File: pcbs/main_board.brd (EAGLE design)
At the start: 120 x 20 mm, 41 parts, among them IC1 317T, IC2 MEGA48/88/168-AU, J1 22-27-2021-02, K1 G6K-2F, Q1 MOSFET-NCHANNELSMD, Q2 MOSFET-NCHANNELSMD

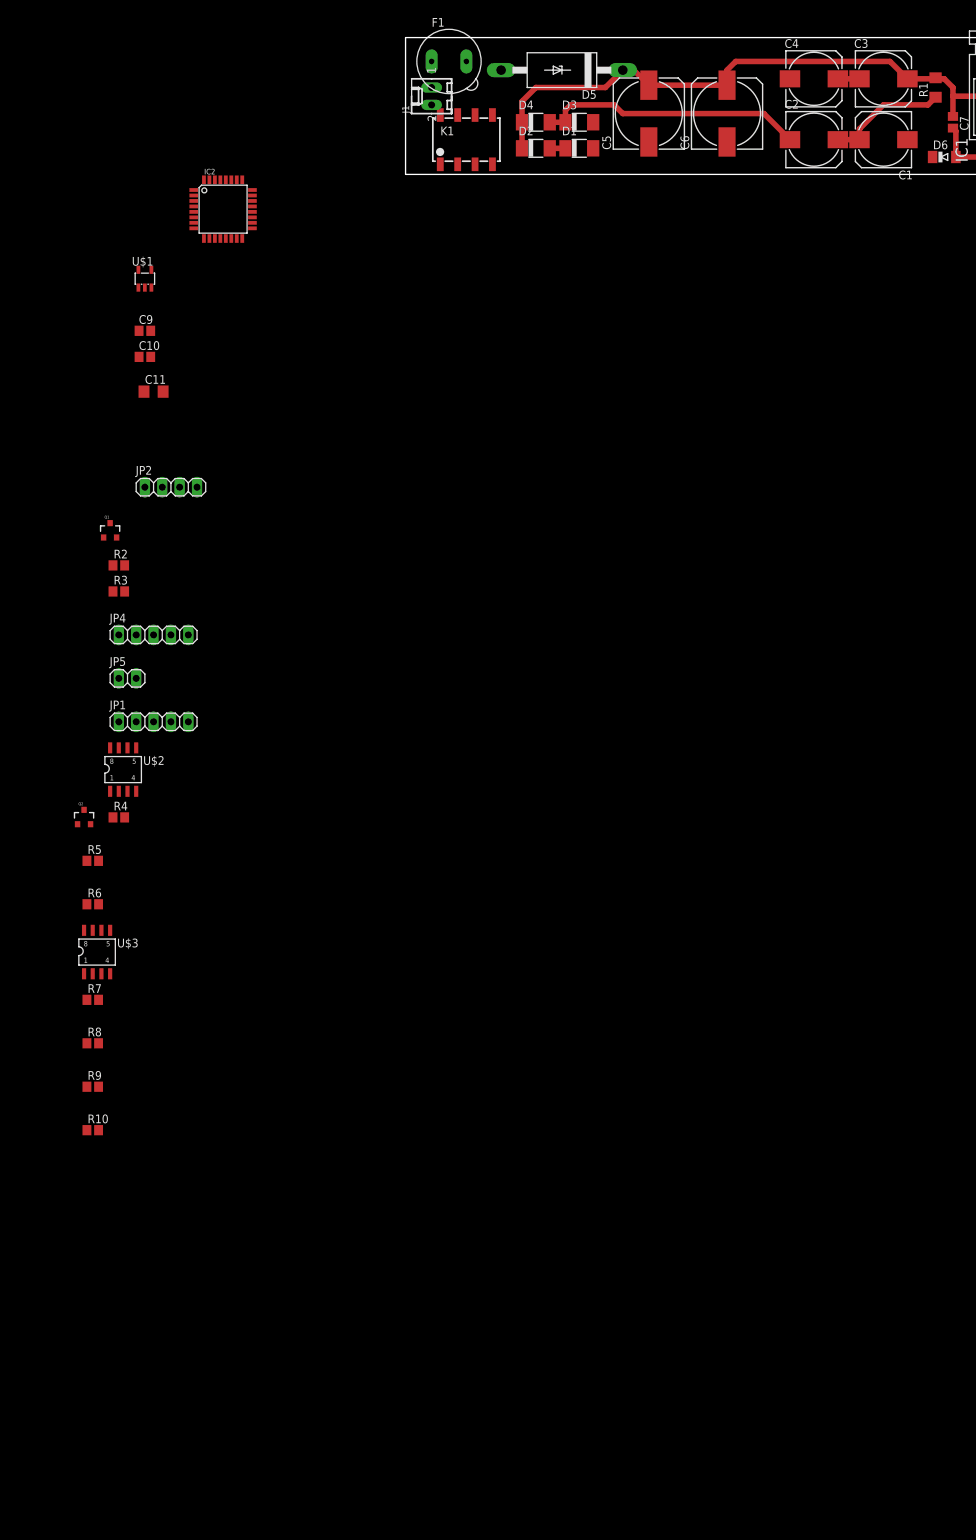
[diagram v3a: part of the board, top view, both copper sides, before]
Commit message: Main Board: Added resistor dividers for voltage measurements.
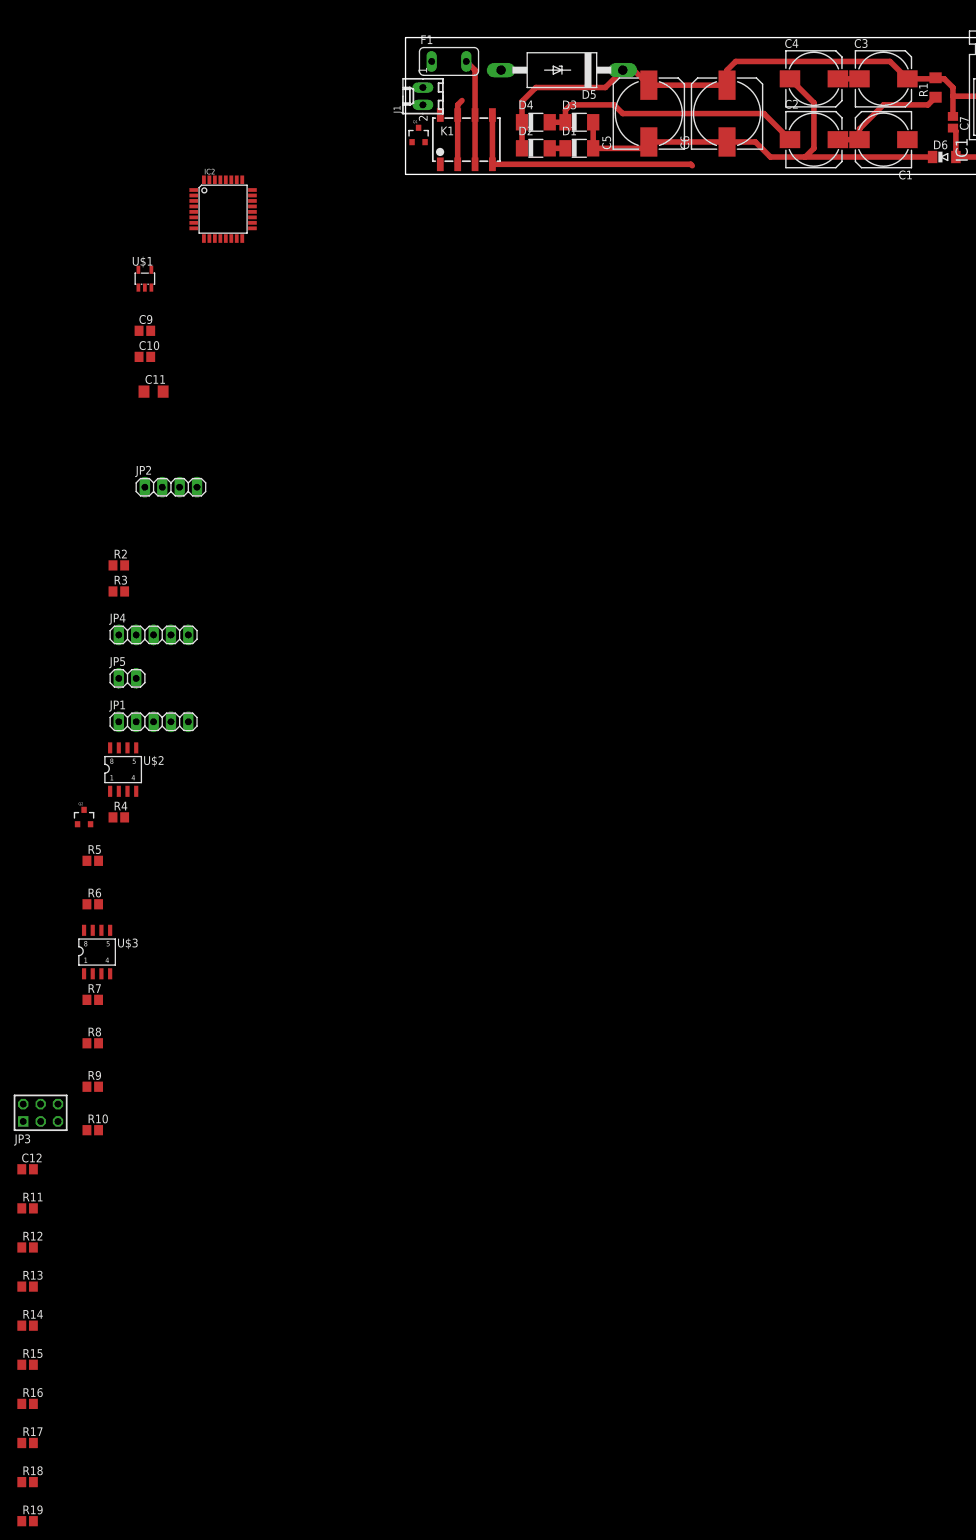
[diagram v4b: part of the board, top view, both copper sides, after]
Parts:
- added C12: 10n, resistor:C0805
- added JP3: AVR-ISP-6VERT, ShortCircuitRobotics:AVR-ISP-6
- added R11, R12, R13, R14, R15, R16, R17, R18: 1k, resistor:R0805
- added R19: 100k, resistor:R0805
- F1: value FUSE19560 -> (none); device fuse:19560 -> fuse:TE5
- moved Q1 73.3 mm to (1.91, 5.71)
- moved J1 1.27 mm to (2.54, 11.4)
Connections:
- removed net N$22: IC2.26
- removed net N$23: IC2.25
- removed net N$24: IC2.24
- removed net N$25: IC2.23
- removed net N$5: C3.+, C5.+, C6.+, C7.1, D2.C, D4.C, D5.C, IC1.3, R1.2
- new net ADC0: IC2.23, R11.2, R12.1
- new net ADC1: IC2.24, R13.2, R14.1
- new net ADC2: IC2.25, R15.2, R16.1
- new net ADC3: IC2.26, R17.2, R18.1
- new net CELL3: R15.1
- new net N$11: C2.-, D3.C, D4.A
- new net N$21: IC2.15, JP3.4
- new net N$7: IC2.17, JP3.3
- new net RESET: IC2.29, JP3.5
- new net V_IN: C3.+, C5.+, C6.+, C7.1, D2.C, D4.C, D5.C, IC1.3, R1.2, R11.1
- net +12V: now also R13.1
- net BATTERY_ON: now also IC2.8
- net FRONT_POWER: now also IC2.19
- net GND: now also C12.2, JP3.6, R12.2, R14.2, R16.2, R18.2
- net INPUT_SEL: now also IC2.7
- net N$1: now also K1.2, K1.7
- net N$12: now also IC2.16, JP3.1; no longer IC2.19
- net N$2: now also C12.1, IC2.20; no longer C2.-, D3.C, D4.A, K1.2, K1.7
- net SPEED_REAR_IN: now also IC2.1
- net SPEED_REAR_OUT: now also IC2.2
- net TAIL_LIGHT: now also R19.2
- net TAIL_POWER: now also IC2.12
- net TAIL_PWM: now also IC2.10
- net VCC: now also JP3.2, R19.1; no longer IC2.20
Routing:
- net V_IN: track 0.00 -> 127.2 mm
- net N$5: track 127.2 -> 0.00 mm
- net GND: track 0.00 -> 68.1 mm
- net N$2: track 39.3 -> 0.00 mm
- net N$11: track 0.00 -> 39.3 mm
- net N$6: track 0.00 -> 36.5 mm
- net N$8: track 0.00 -> 15.6 mm
- net N$1: track 3.16 -> 12.7 mm

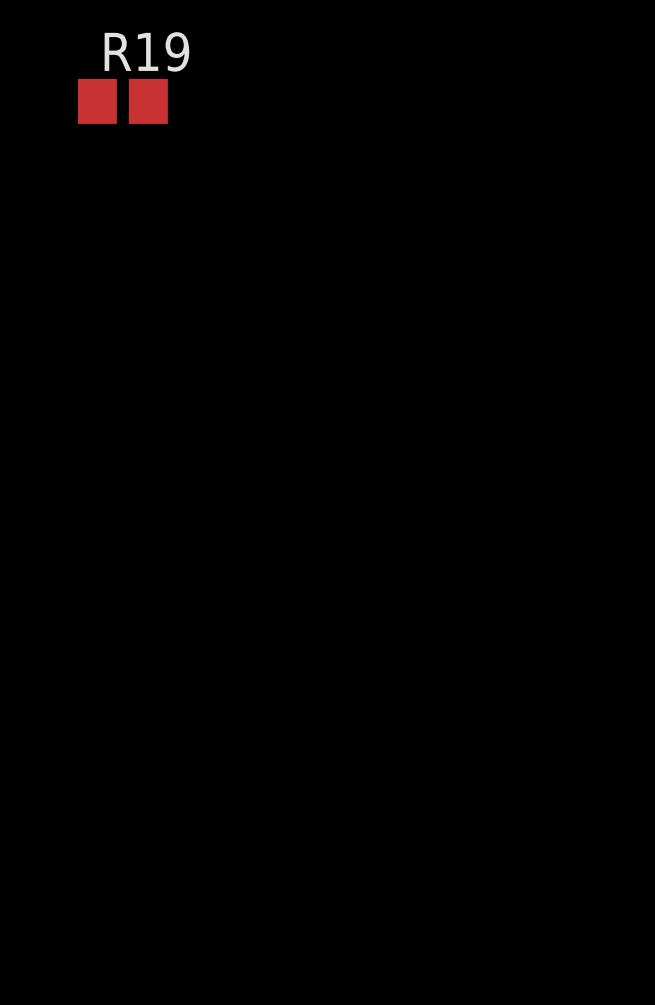
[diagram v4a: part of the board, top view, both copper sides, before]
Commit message: Main Board: Added switchable 12V output.
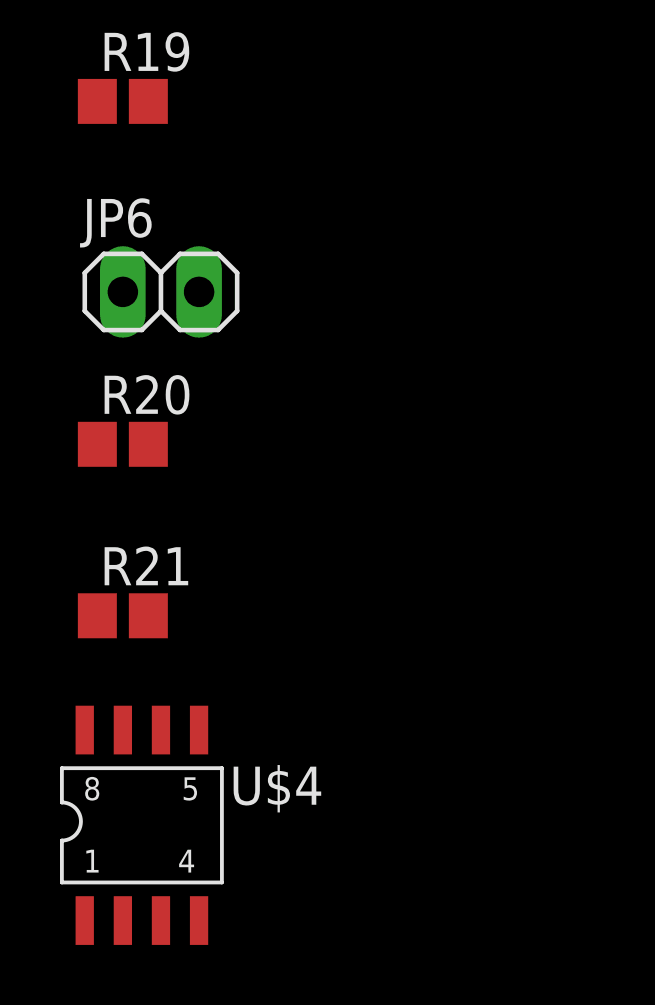
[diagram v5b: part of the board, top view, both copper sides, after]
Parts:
- added JP6: (no value), pinhead:1X02
- added R20: 100k, resistor:R0805
- added R21: 1k, resistor:R0805
- added U$4: IRF7413, ShortCircuitRobotics:SO8-2
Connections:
- new net 12V_OUT_ON: IC2.11, R21.1
- new net N$22: R20.1, R21.2, U$4.4
- new net N$5: JP6.2, U$4.5, U$4.6, U$4.7, U$4.8
- net +12V: now also JP6.1
- net GND: now also R20.2, U$4.1, U$4.2, U$4.3
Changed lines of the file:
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@@
 <element name="R18" library="resistor" package="R0805" value="1k" x="-55.245" y="-191.135"/>
 <element name="R19" library="resistor" package="R0805" value="100k" x="-55.245" y="-196.85"/>
+<element name="JP6" library="pinhead" package="1X02" value="" x="-53.975" y="-203.2"/>
+<element name="R20" library="resistor" package="R0805" value="100k" x="-55.245" y="-208.28"/>
+<element name="R21" library="resistor" package="R0805" value="1k" x="-55.245" y="-213.995"/>
+<element name="U$4" library="ShortCircuitRobotics" package="SO8-2" value="IRF7413" x="-53.975" y="-221.615"/>
 </elements>
 <signals>
@@
 <contactref element="R16" pad="2"/>
 <contactref element="R18" pad="2"/>
+<contactref element="U$4" pad="2"/>
+<contactref element="U$4" pad="1"/>
+<contactref element="U$4" pad="3"/>
+<contactref element="R20" pad="2"/>
 <wire x1="-54.395" y1="-179.705" x2="-54.395" y2="-191.135" width="0" layer="19" extent="1-1"/>
 <wire x1="-54.395" y1="-168.275" x2="-54.395" y2="-179.705" width="0" layer="19" extent="1-1"/>
@@
 <wire x1="-44.87" y1="-100.33" x2="-44.45" y2="-116.84" width="0" layer="19" extent="1-1"/>
 <wire x1="-46.04" y1="-94.98" x2="-44.87" y2="-100.33" width="0" layer="19" extent="1-1"/>
+<wire x1="-54.395" y1="-208.28" x2="-54.395" y2="-191.135" width="0" layer="19" extent="1-1"/>
+<wire x1="-53.975" y1="-224.155" x2="-54.395" y2="-208.28" width="0" layer="19" extent="1-1"/>
+<wire x1="-55.245" y1="-224.155" x2="-53.975" y2="-224.155" width="0" layer="19" extent="1-1"/>
+<wire x1="-56.515" y1="-224.155" x2="-55.245" y2="-224.155" width="0" layer="19" extent="1-1"/>
 <wire x1="-31.75" y1="-67.31" x2="-46.04" y2="-94.98" width="0" layer="19" extent="1-1"/>
 <wire x1="-42.76" y1="-57.15" x2="-31.75" y2="-67.31" width="0" layer="19" extent="1-1"/>
@@
 <contactref element="JP2" pad="1"/>
 <contactref element="R13" pad="1"/>
+<contactref element="JP6" pad="1"/>
+<wire x1="-55.245" y1="-203.2" x2="-56.095" y2="-162.56" width="0" layer="19" extent="1-1"/>
 <wire x1="-41.06" y1="-93.98" x2="-56.095" y2="-162.56" width="0" layer="19" extent="1-1"/>
 <wire x1="-40.64" y1="-90.17" x2="-41.06" y2="-93.98" width="0" layer="19" extent="1-1"/>
@@
 <contactref element="R15" pad="1"/>
 </signal>
+<signal name="N$5">
+<contactref element="JP6" pad="2"/>
+<contactref element="U$4" pad="6"/>
+<contactref element="U$4" pad="5"/>
+<contactref element="U$4" pad="8"/>
+<contactref element="U$4" pad="7"/>
+<wire x1="-55.245" y1="-217.805" x2="-56.515" y2="-217.805" width="0" layer="19" extent="1-1"/>
+<wire x1="-53.975" y1="-217.805" x2="-55.245" y2="-217.805" width="0" layer="19" extent="1-1"/>
+<wire x1="-52.705" y1="-217.805" x2="-53.975" y2="-217.805" width="0" layer="19" extent="1-1"/>
+<wire x1="-52.705" y1="-203.2" x2="-52.705" y2="-217.805" width="0" layer="19" extent="1-1"/>
+</signal>
+<signal name="N$22">
+<contactref element="R21" pad="2"/>
+<contactref element="R20" pad="1"/>
+<contactref element="U$4" pad="4"/>
+<wire x1="-54.395" y1="-213.995" x2="-52.705" y2="-224.155" width="0" layer="19" extent="1-1"/>
+<wire x1="-56.095" y1="-208.28" x2="-54.395" y2="-213.995" width="0" layer="19" extent="1-1"/>
+</signal>
+<signal name="12V_OUT_ON">
+<contactref element="R21" pad="1"/>
+<contactref element="IC2" pad="11"/>
+<wire x1="-56.095" y1="-213.995" x2="-27.87" y2="-9.3726" width="0" layer="19" extent="1-1"/>
+</signal>
 </signals>

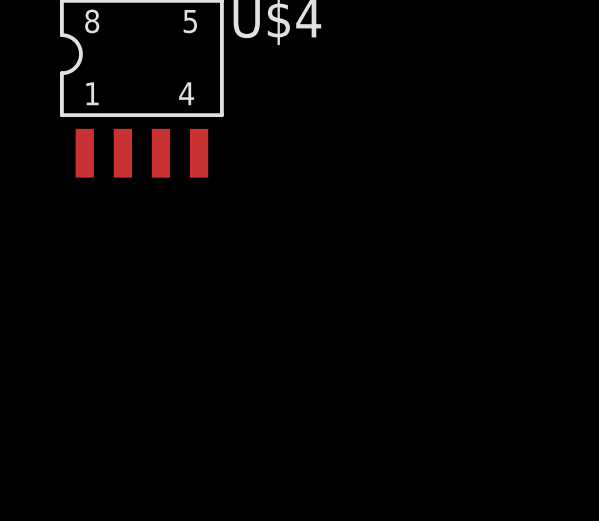
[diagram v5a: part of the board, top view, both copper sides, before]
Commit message: Main Board: added i2c pullups.
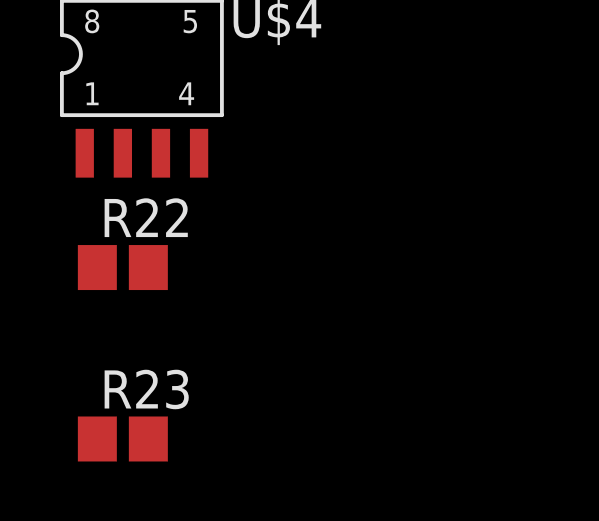
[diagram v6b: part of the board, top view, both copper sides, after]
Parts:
- added R22: 4.7k, resistor:R0805
- added R23: 4,7k, resistor:R0805
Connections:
- net FRONT_SCL: now also R22.1
- net FRONT_SDA: now also R23.1
- net VCC: now also R22.2, R23.2
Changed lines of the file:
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@@
 <element name="R21" library="resistor" package="R0805" value="1k" x="-55.245" y="-213.995"/>
 <element name="U$4" library="ShortCircuitRobotics" package="SO8-2" value="IRF7413" x="-53.975" y="-221.615"/>
+<element name="R22" library="resistor" package="R0805" value="4.7k" x="-55.245" y="-227.965"/>
+<element name="R23" library="resistor" package="R0805" value="4,7k" x="-55.245" y="-233.68"/>
 </elements>
 <signals>
@@
 <contactref element="JP3" pad="2"/>
 <contactref element="R19" pad="1"/>
+<contactref element="R22" pad="2"/>
+<contactref element="R23" pad="2"/>
+<wire x1="-54.395" y1="-227.965" x2="-56.095" y2="-196.85" width="0" layer="19" extent="1-1"/>
+<wire x1="-54.395" y1="-233.68" x2="-54.395" y2="-227.965" width="0" layer="19" extent="1-1"/>
 <wire x1="-55.88" y1="-135.89" x2="-56.095" y2="-196.85" width="0" layer="19" extent="1-1"/>
 <wire x1="-39.37" y1="-80.01" x2="-55.88" y2="-135.89" width="0" layer="19" extent="1-1"/>
@@
 <contactref element="JP1" pad="3"/>
 <contactref element="IC2" pad="27"/>
+<contactref element="R23" pad="1"/>
 <wire x1="-25.47" y1="-0.7874" x2="-36.83" y2="-80.01" width="0" layer="19" extent="1-1"/>
+<wire x1="-56.095" y1="-233.68" x2="-36.83" y2="-80.01" width="0" layer="19" extent="1-1"/>
 </signal>
 <signal name="FRONT_SCL">
 <contactref element="JP1" pad="4"/>
 <contactref element="IC2" pad="28"/>
+<contactref element="R22" pad="1"/>
 <wire x1="-26.27" y1="-0.7874" x2="-34.29" y2="-80.01" width="0" layer="19" extent="1-1"/>
+<wire x1="-56.095" y1="-227.965" x2="-34.29" y2="-80.01" width="0" layer="19" extent="1-1"/>
 </signal>
 <signal name="CELL_3">
